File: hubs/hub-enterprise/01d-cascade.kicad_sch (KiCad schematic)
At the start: 6 parts, among them U104 TPS2121RUXR, U105 TPS2121RUXR

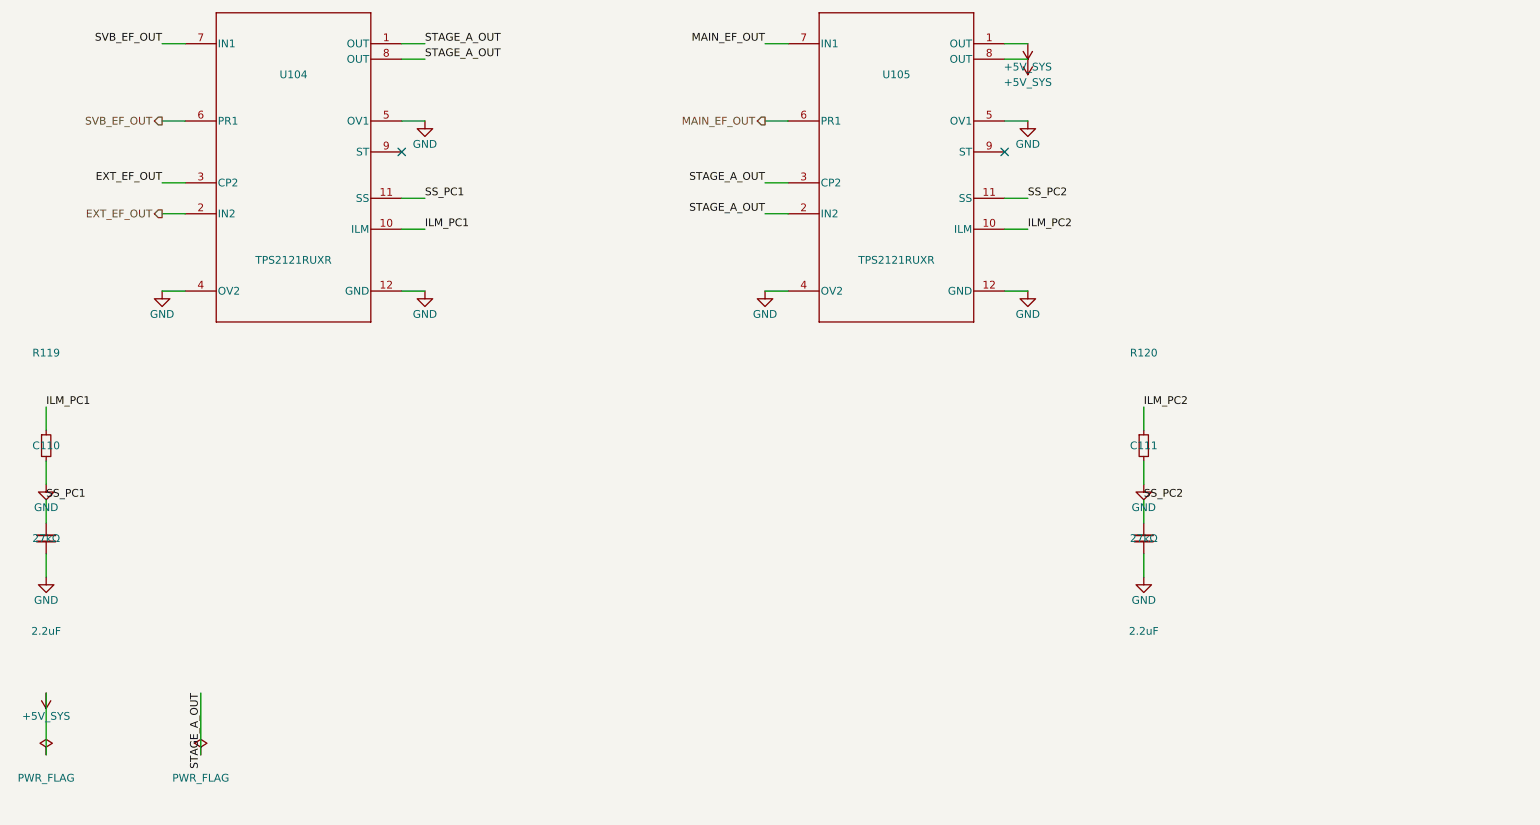
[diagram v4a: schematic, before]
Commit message: T1 composition pass: centered sheets, wired decouplers, drawn structure
Owner ask applied across the generated ENT hub sheets: content is
centered on the page (leaves moved A3->A4), decoupling caps sit at
their owner IC and connect by real drawn Manhattan wires instead of
floating label aliases, divider chains / pull-ups / ILIM parts are
drawn structure, and the thin parent is a genuine flow diagram --
per-side sheet pins, real eFuse->cascade fan-in wires on collision-free
lanes, EXT_5V routed to rail-sense with a junctioned tap, sheet-pin
names rendered inside their boxes (the owner-visible garble was the
justify convention, measured and fixed).

Mechanisms: build_leaf consumes a composed layout (wires, hier_at
overrides, decoupler rails, per-part text side) with a content-bbox
centering pass, geometry-aware Ref/Value placement, auto-junctions,
and away-side power stamps; per-leaf compose_*() in the generator (one
eFuse template drives 01a/b/c; 01e runs place_decouplers/
wire_decouplers verbatim); nudge_texts as the finishing pass. The
parent's box geometry is grid-aligned so sheet pins sit both on-edge
and on-grid -- the entire endpoint_off_grid ERC class is gone (19->0).

Real T1 bug found via render iteration: property bboxes must be
computed at the RENDERED angle (symbol rotation + field angle) -- a
rot-90 inductor's value was bboxed vertical, false-collided, and got
nudged 40mm away. Fixed in cec_sch_layout with RotatedFieldBBoxTest
(12/12).

Gates, all verified independently: netlist identity 0 missing/0 extra
(59 components, 46 groups, checker exit 0); ERC 4 benign classes only,
no annotation warning; overlaps 0 on all 8 generated sheets (was 45
pairs); lint ERROR 0 (was 38), 15 documented SL-04 WARNs. Charter T1
row: integration DONE; gates 5/6 ADOPTED into the per-sheet protocol.

Co-Authored-By: Claude Fable 5 <noreply@anthropic.com>
Claude-Session: https://claude.ai/code/session_011q5bmwF5BFtSf8Ft5vT1DZ
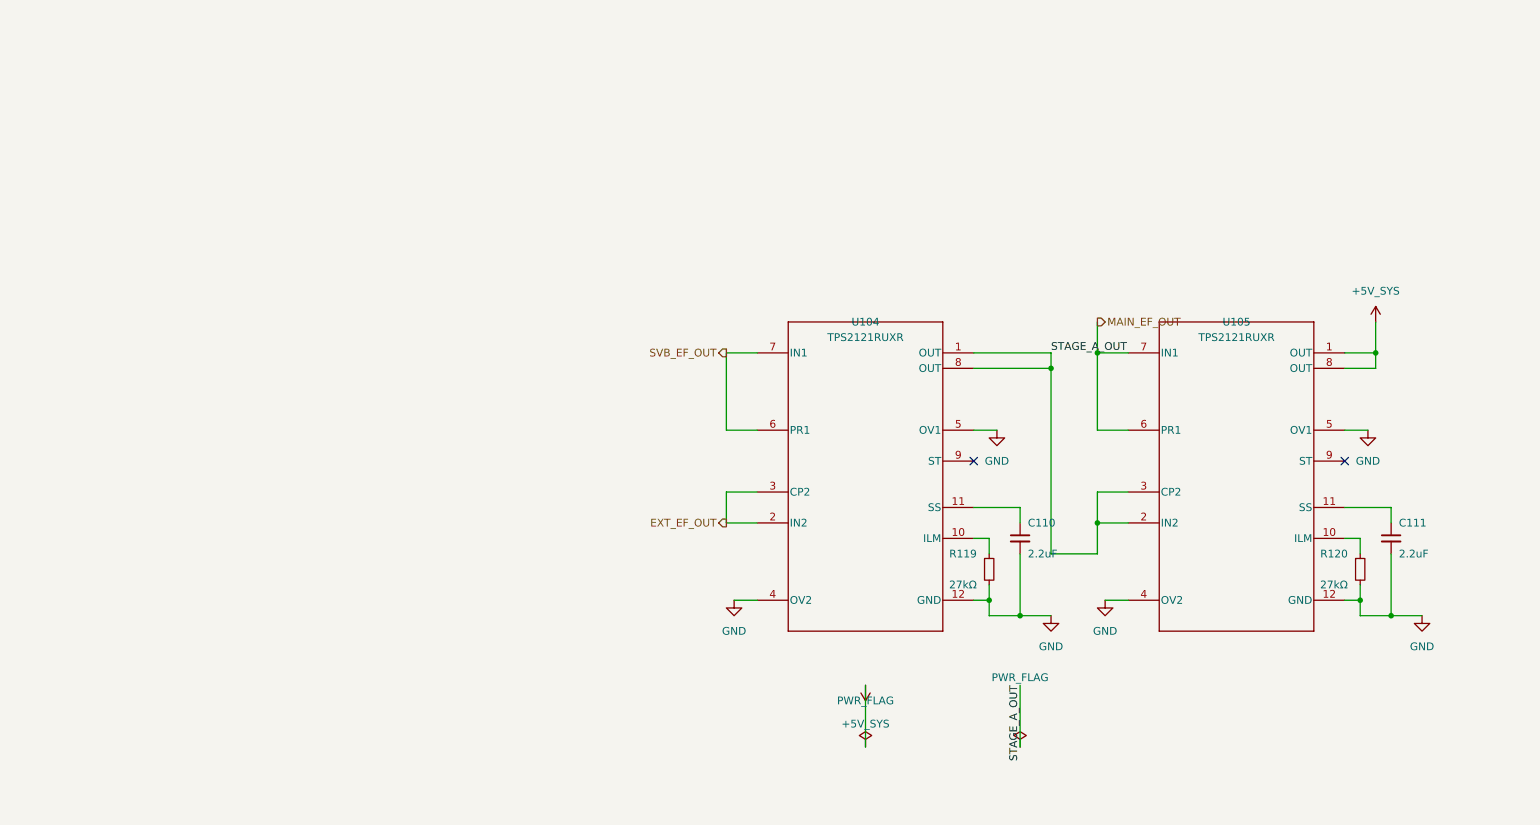
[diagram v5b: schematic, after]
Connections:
- net ILM_PC1: no longer names the net of R119.1, U104.10 (ILM)
- net ILM_PC2: no longer names the net of R120.1, U105.10 (ILM)
- net SS_PC1: no longer names the net of C110.1, U104.11 (SS)
- net SS_PC2: no longer names the net of C111.1, U105.11 (SS)

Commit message: WIP snapshot: composition agent hub regeneration in flight (durability)
Co-Authored-By: Claude Fable 5 <noreply@anthropic.com>
Claude-Session: https://claude.ai/code/session_011q5bmwF5BFtSf8Ft5vT1DZ
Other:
- note added: "PR1->IN1 + CP2->IN2 per the AS-BUILT hub-standard netlist (BOM-D's CP2->GND was flagged unverified by its own author)"
- note added: "Priority cascade (2x TPS2121): 5VSB>EXT stage A, MAIN_5V>stage-A-out stage B"

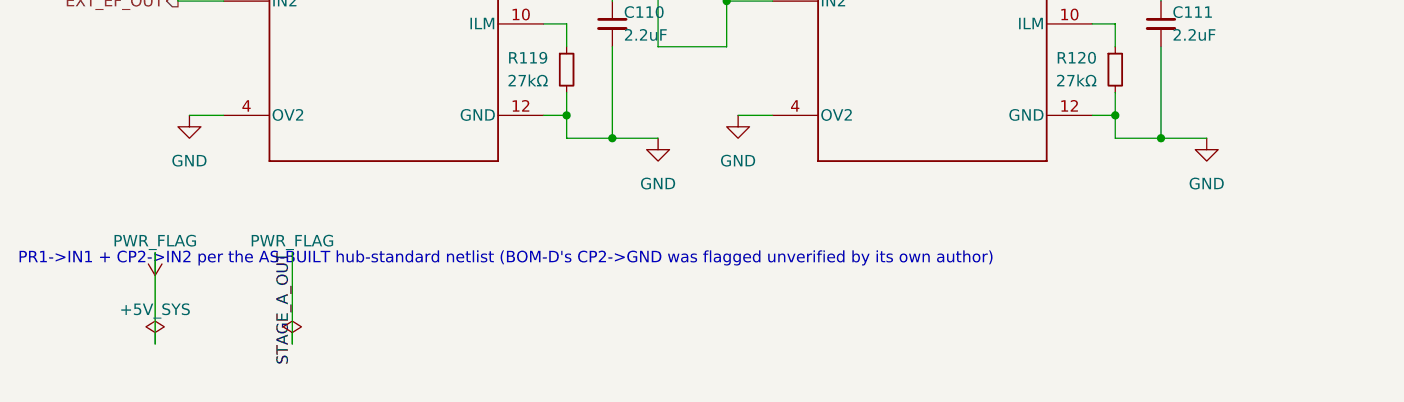
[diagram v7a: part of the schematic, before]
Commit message: WIP snapshot: composition agent iterating (durability)
Co-Authored-By: Claude Fable 5 <noreply@anthropic.com>
Claude-Session: https://claude.ai/code/session_011q5bmwF5BFtSf8Ft5vT1DZ
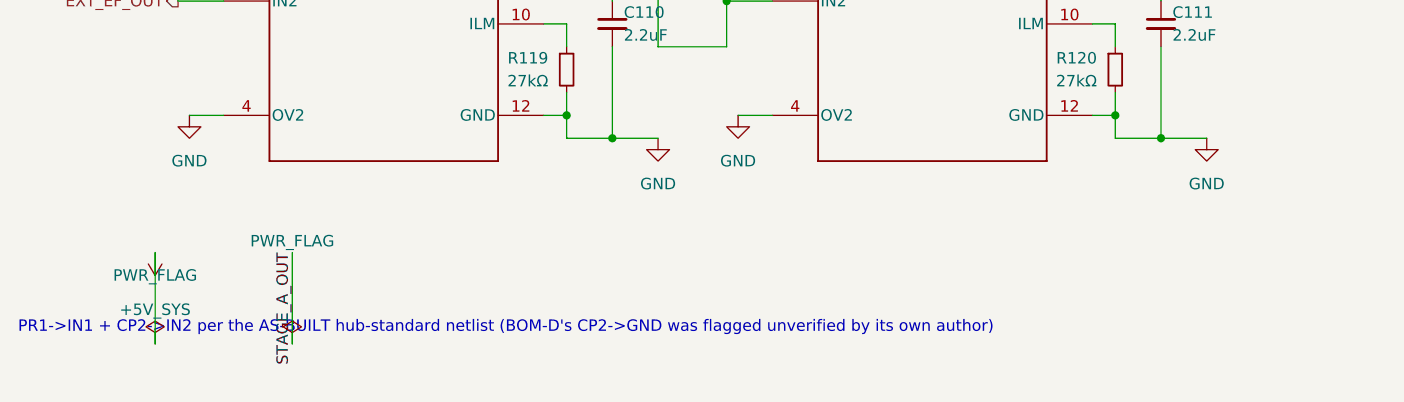
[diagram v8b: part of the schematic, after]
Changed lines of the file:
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@@
 	(text "PR1->IN1 + CP2->IN2 per the AS-BUILT hub-standard netlist (BOM-D's CP2->GND was flagged unverified by its own author)"
 		(exclude_from_sim no)
-		(at 71.12 130.81 0)
+		(at 71.12 138.43 0)
 		(effects (font (size 1.27 1.27) (color 21 96 61 1)) (justify left top))
 	)
@@
 		(dnp no)
 		(property "Reference" "#FLG409" (at 86.36 138.43 0) (effects (font (size 1.27 1.27)) (hide yes)))
-		(property "Value" "PWR_FLAG" (at 86.36 129.54 0) (effects (font (size 1.27 1.27))))
-		(pin "1")
-		(instances
+		(property "Value" "PWR_FLAG" (at 86.36 133.35 0) (effects (font (size 1.27 1.27))))
+		(pin "1")
+		(instances
